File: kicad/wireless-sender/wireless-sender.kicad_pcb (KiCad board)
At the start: 2 copper layers, 38.1 x 28.2 mm, 18 parts, among them J1 Pedals, J2 Battery

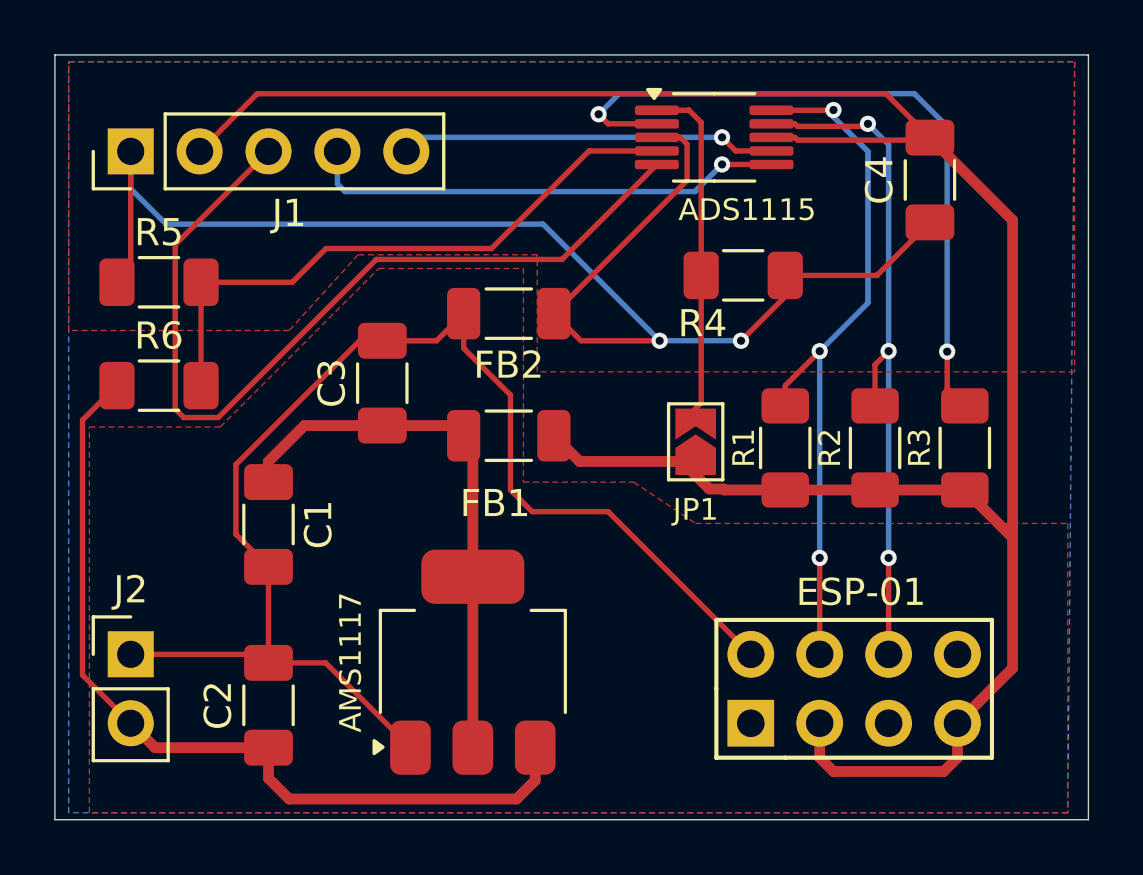
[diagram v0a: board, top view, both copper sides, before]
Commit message: PCB Update
Replaced AMS1117 with HT7333.
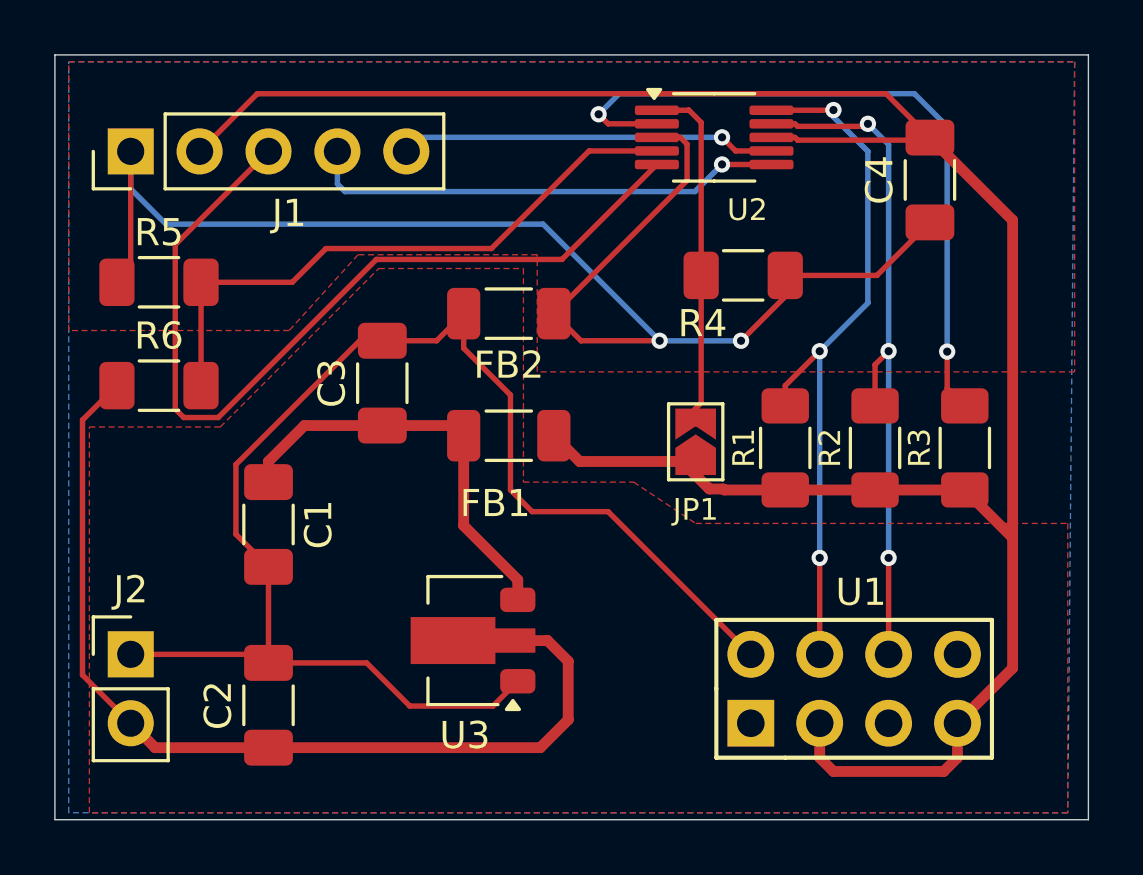
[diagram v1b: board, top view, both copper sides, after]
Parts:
- removed AMS1117: AMS1117-3.3, Package_TO_SOT_SMD:SOT-223-3_TabPin2
- added U3: HT7333-SOT89, Package_TO_SOT_SMD:SOT-89-3, F.Cu at (101.2, 98.6)
- renumbered ESP-01 to U1, ADS1115 to U2
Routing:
- net +3.3V: track 20.3 -> 16.0 mm
- net GND: track 48.8 -> 52.5 mm
- net +BATT: track 31.9 -> 35.1 mm
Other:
- board text added: "v0.2 - Aug. 2025"
- board text removed: "v0.1 - Aug. 2025"
